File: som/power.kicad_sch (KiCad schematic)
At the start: 1 part, among them U1 XC7A200T-3FBG484E

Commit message: Mezz Power Tweak Ok
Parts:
- added C10, C11, C12, C13, C14, C15, C16, C17, C18, C19, C20, C21, C22, C23, C24, C25, C26, C27, C28, C29, C3, C30, C31, C4, C5, C6, C7, C8, C9: 100nF, Capacitor_SMD:C_0402_1005Metric_Pad0.74x0.62mm_HandSolder, symbol Device:C_Small
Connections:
- net +1V0: now also C3.1, C30.1, C31.1, C4.1, C5.1, C6.1, C7.1, C8.1, C9.1
- net +1V35: now also C12.1, C13.1, C14.1, C15.1, C16.1, C17.1
- net +1V8: now also C10.1, C11.1
- net +3V3: now also C27.1
- net GND: now also C10.2, C11.2, C12.2, C13.2, C14.2, C15.2, C16.2, C17.2, C18.2, C19.2, C20.2, C21.2, C22.2, C23.2, C24.2, C25.2, C26.2, C27.2, C28.2, C29.2, C3.2, C30.2, C31.2, C4.2, C5.2, C6.2, C7.2, C8.2, C9.2
- net VBANK13: now also C28.1, C29.1
- net VBANK14: now also C24.1, C25.1, C26.1
- net VBANK15: now also C21.1, C22.1, C23.1
- net VBANK16: now also C18.1, C19.1, C20.1
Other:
- moved on the sheet: U1J

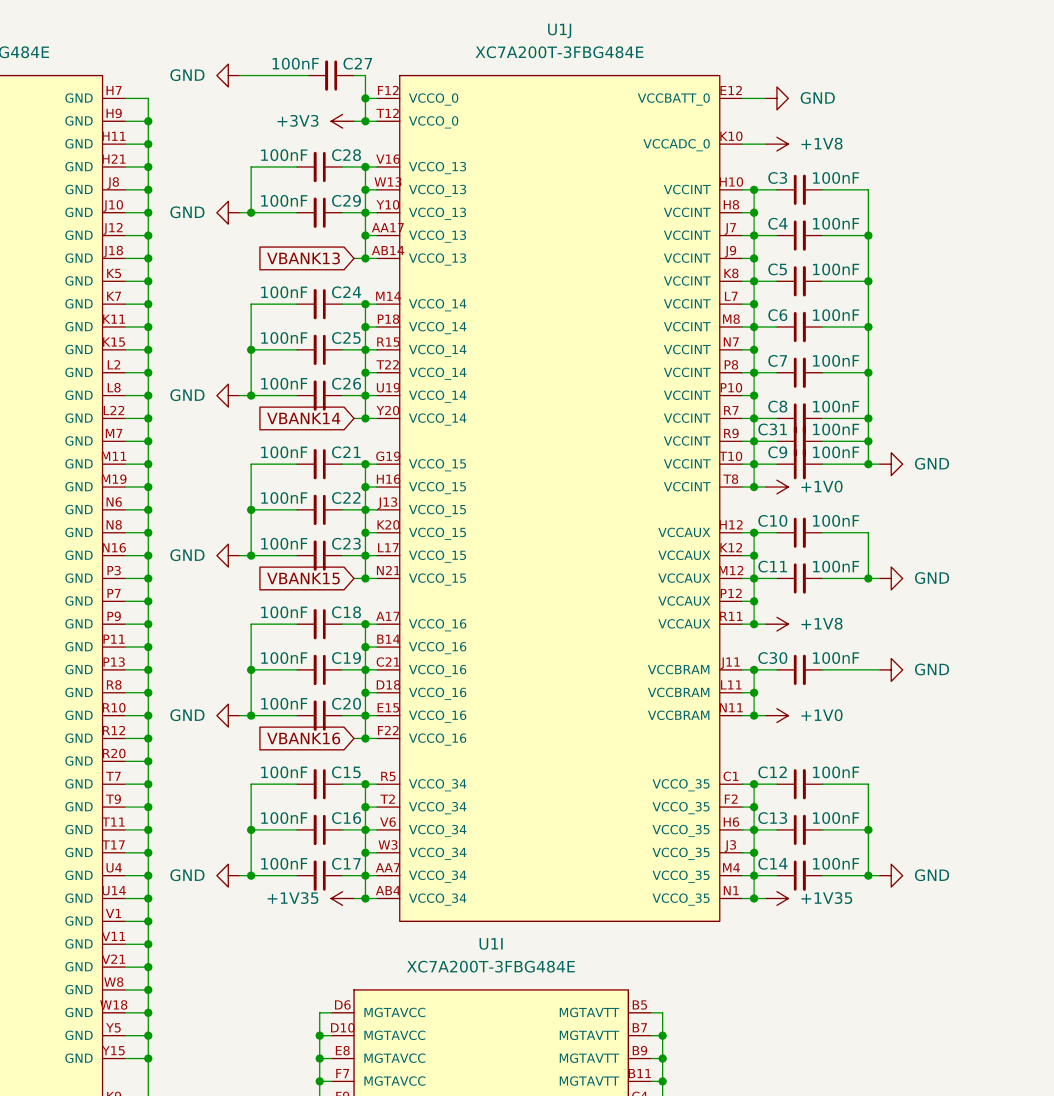
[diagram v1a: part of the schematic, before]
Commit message: Le DDR3 control traces
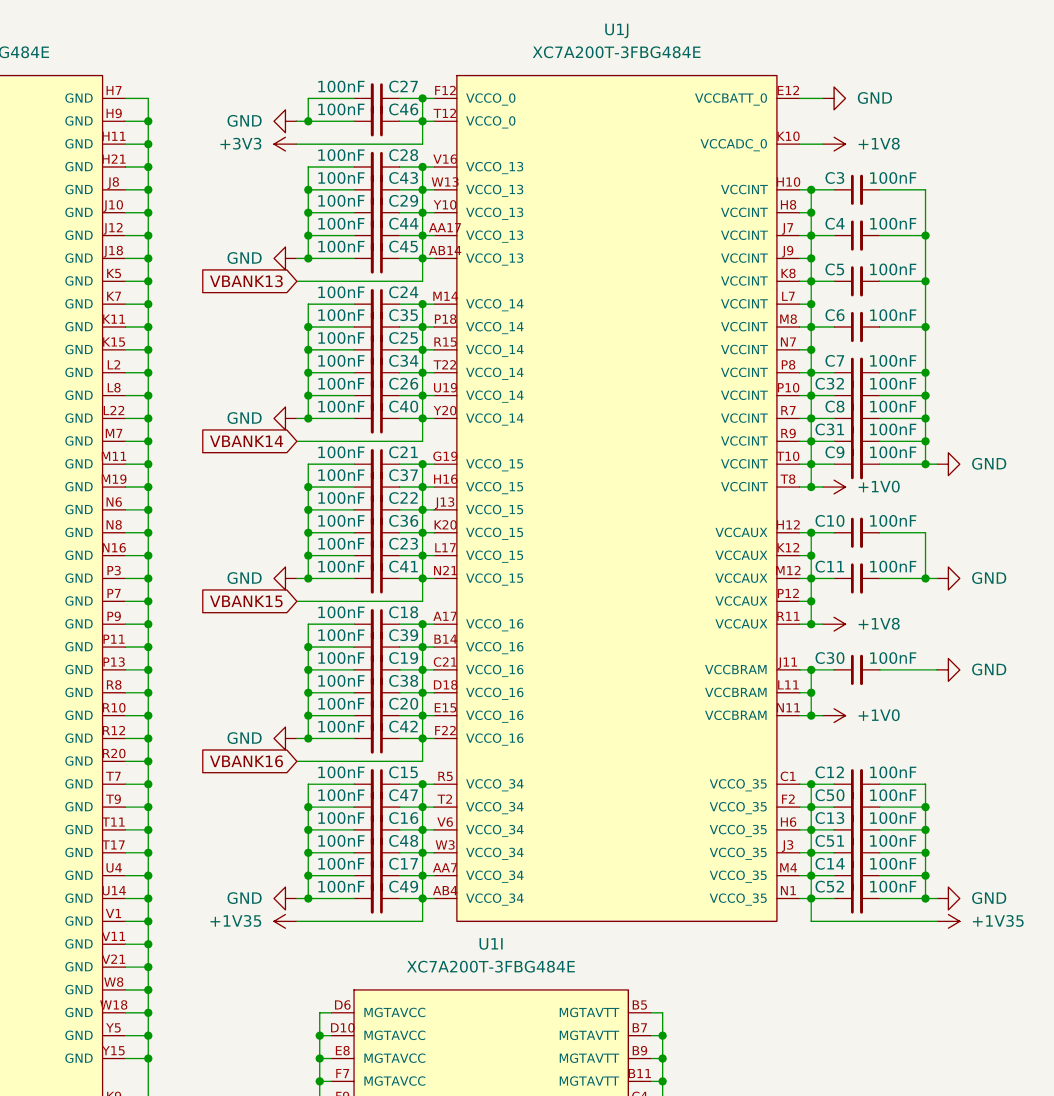
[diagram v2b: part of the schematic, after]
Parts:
- added C32, C34, C35, C36, C37, C38, C39, C40, C41, C42, C43, C44, C45, C46, C47, C48, C49, C50, C51, C52: 100nF, Capacitor_SMD:C_0402_1005Metric, symbol Device:C_Small
- C10, C11, C12, C13, C14, C15, C16, C17, C18, C19, C20, C21, C22, C23, C24, C25, C26, C27, C28, C29, C3, C30, C31, C4, C5, C6, C7, C8, C9: footprint Capacitor_SMD:C_0402_1005Metric_Pad0.74x0.62mm_HandSolder -> Capacitor_SMD:C_0402_1005Metric
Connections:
- net +1V0: now also C32.1
- net +1V35: now also C47.1, C48.1, C49.1, C50.1, C51.1, C52.1
- net +3V3: now also C46.1
- net GND: now also C32.2, C34.2, C35.2, C36.2, C37.2, C38.2, C39.2, C40.2, C41.2, C42.2, C43.2, C44.2, C45.2, C46.2, C47.2, C48.2, C49.2, C50.2, C51.2, C52.2
- net VBANK13: now also C43.1, C44.1, C45.1
- net VBANK14: now also C34.1, C35.1, C40.1
- net VBANK15: now also C36.1, C37.1, C41.1
- net VBANK16: now also C38.1, C39.1, C42.1
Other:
- moved on the sheet: C10, C11, C12, C13, C14, C15, C16, C17, C18, C19, C20, C21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

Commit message: I really should commit when I make it and not a month later
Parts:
- added C58, C59, C60, C61, C62: 100nF, Capacitor_SMD:C_0402_1005Metric, symbol Device:C_Small
- added C63: 1500uF, Capacitor_SMD:CP_Elec_10x10.5, symbol Device:C_Polarized_Small
- added C64, C65, C66, C67, C68, C69, C70, C71, C72, C73, C74, C75, C76, C77, C78, C79, C80, C81, C82, C83, C84, C85: 10uF, Capacitor_SMD:C_0402_1005Metric, symbol Device:C_Small
- added L1, L2: 2uH, Inductor_SMD:L_7.3x7.3_H3.5, symbol Device:L_Small
- added R10, R6: 75K, Resistor_SMD:R_0402_1005Metric_Pad0.72x0.64mm_HandSolder, symbol Device:R_Small
- added R11, R12, R13, R14, R9: 20K, Resistor_SMD:R_0402_1005Metric_Pad0.72x0.64mm_HandSolder, symbol Device:R_Small
- added R7: 300K, Resistor_SMD:R_0402_1005Metric_Pad0.72x0.64mm_HandSolder, symbol Device:R_Small
- added R8: 30K, Resistor_SMD:R_0402_1005Metric_Pad0.72x0.64mm_HandSolder, symbol Device:R_Small
- added U5: SIC402, SIC402:SIC402, symbol SIC402:SIC402
- added U6: TLV62569PDRLR, Package_SON:WSON-6_1.5x1.5mm_P0.5mm, symbol Regulator_Switching:TLV62569DDC
- C10, C11, C12, C13, C14, C15, C16, C17, C18, C19, C20, C21, C22, C23, C24, C25, C26, C27, C28, C29, C3, C30, C31, C32, C34, C35, C36, C37, C38, C39, C4, C40, C41, C42, C43, C44, C45, C46, C47, C48, C49, C5, C50, C51, C52, C6, C7, C8, C9: value 100nF -> 10uF
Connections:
- net +1V0: now also C63.1, C64.1, C65.1, C66.1, C67.1, C68.1, C69.1, C70.1, C75.1, C76.1, C77.1, C78.1, C79.1, L1.2, R9.2, U5.2 (VOUT)
- net +1V2: now also C80.1, C81.1, C82.1, C83.1, C84.1, C85.1
- net +1V8: now also C71.1, C72.1, C73.1, C74.1
- net +3V3: now also C61.1, C62.1, L2.2, R13.2
- net GND renamed AGND
- net AGND: now also C59.2, C60.2, C62.2, C63.2, C64.2, C65.2, C66.2, C67.2, C68.2, C69.2, C70.2, C71.2, C72.2, C73.2, C74.2, C75.2, C76.2, C77.2, C78.2, C79.2, C80.2, C81.2, C82.2, C83.2, C84.2, C85.2, R14.1, R7.1, R8.1, U5.15 (PNGD), U5.16 (PNGD), U5.17 (PNGD), U5.18 (PNGD), U5.19 (PNGD), U5.20 (PNGD), U5.21 (PNGD), U5.22 (PNGD), U5.30 (AGND), U5.32 (ENL), U5.33 (AGND), U5.4 (AGND), U6.2 (GND)
- new net: R10.1, U5.8 (BST)
- new net: R10.2, U5.13 (LXBST)
- new net: R6.1, R7.2
- new net: R6.2, U5.31 (TON)
- new net: C61.2, R13.1, R14.2, U6.6 (FB)
- new net: L2.1, U6.3 (SW)
- new net: R8.2, R9.1, U5.1 (FB)
- new net: C59.1, U5.7 (SS)
- new net: C58.1, U5.28 (LXS)
- new net: C58.2, U5.27 (ILIM)
- new net: L1.1, U5.23 (LX), U5.24 (LX), U5.25 (LX), U5.35 (LX)
- new net P_{good,1v0}: R11.2, U5.26 (PGOOD)
- new net P_{good,1v8}: R12.2, U6.1 (EN)
- new net P_{good,3v3}: U6.5 (PG)
- new net VIN: C60.1, R11.1, R12.1, U5.10 (VIN), U5.11 (VIN), U5.3 (VDD), U5.34 (VIN), U5.6 (VIN), U5.9 (VIN), U6.4 (VIN)
- no-connect marks 0 -> 2
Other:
- note added: "Main SMP targets: V_{out} = 1.0V I_{ripple} = 1.0A f_{sw} = 500kHz SIC402 formulas: V_{out} = 0.6 * (1 + R_{1}/R_{2}) k = (V_{DD} - 1.75) * 10 / V_{in} R_{ton} = k / 25 pF / f_{sw} t_{on} = V_{out} / V_{in,max} / f_{SW} L = (V_{in} - V_{out}) * t_{on} / I_{ripple} Evaluated: R_{1}/R_{2} = 0.666666667 ~= 20k/30k k = 4.696969697 ~= 4.7 R_{ton} = 375757.575757576 ~= 375k t_{on} = 0.000000606 ~= 60.6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"
- note added: "Power rail summary: - 5.0 v 3.0 A input - 3.3 v 0.5 A output - 1.8 v 0.5 A output - 1.35 v 0.5 A output - 1.2 v 0.5 A output - 1.0 v 10.0 A local"
- note added: "Power sequencing: - 1v0 - 1v8 - 1v35, 1v2, 3v3"
- moved on the sheet: C10, C11, C12, C13, C14, C15, C16, C17, C18, C19, C20, C21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

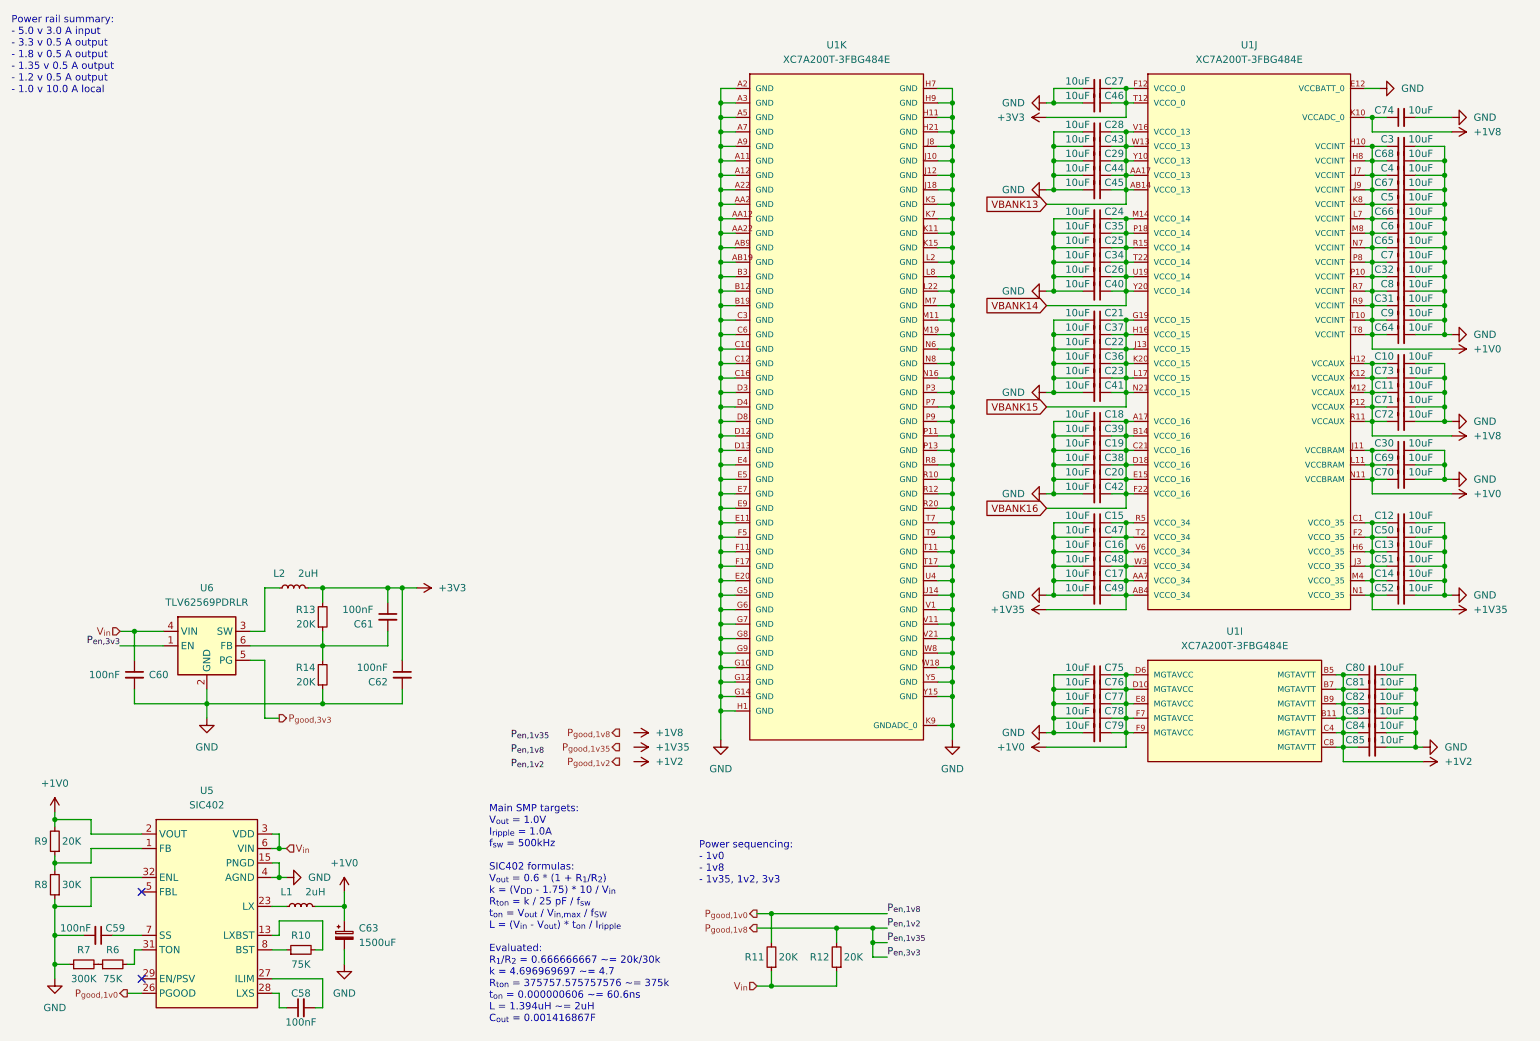
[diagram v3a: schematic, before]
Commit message: Fix the capacitor problem
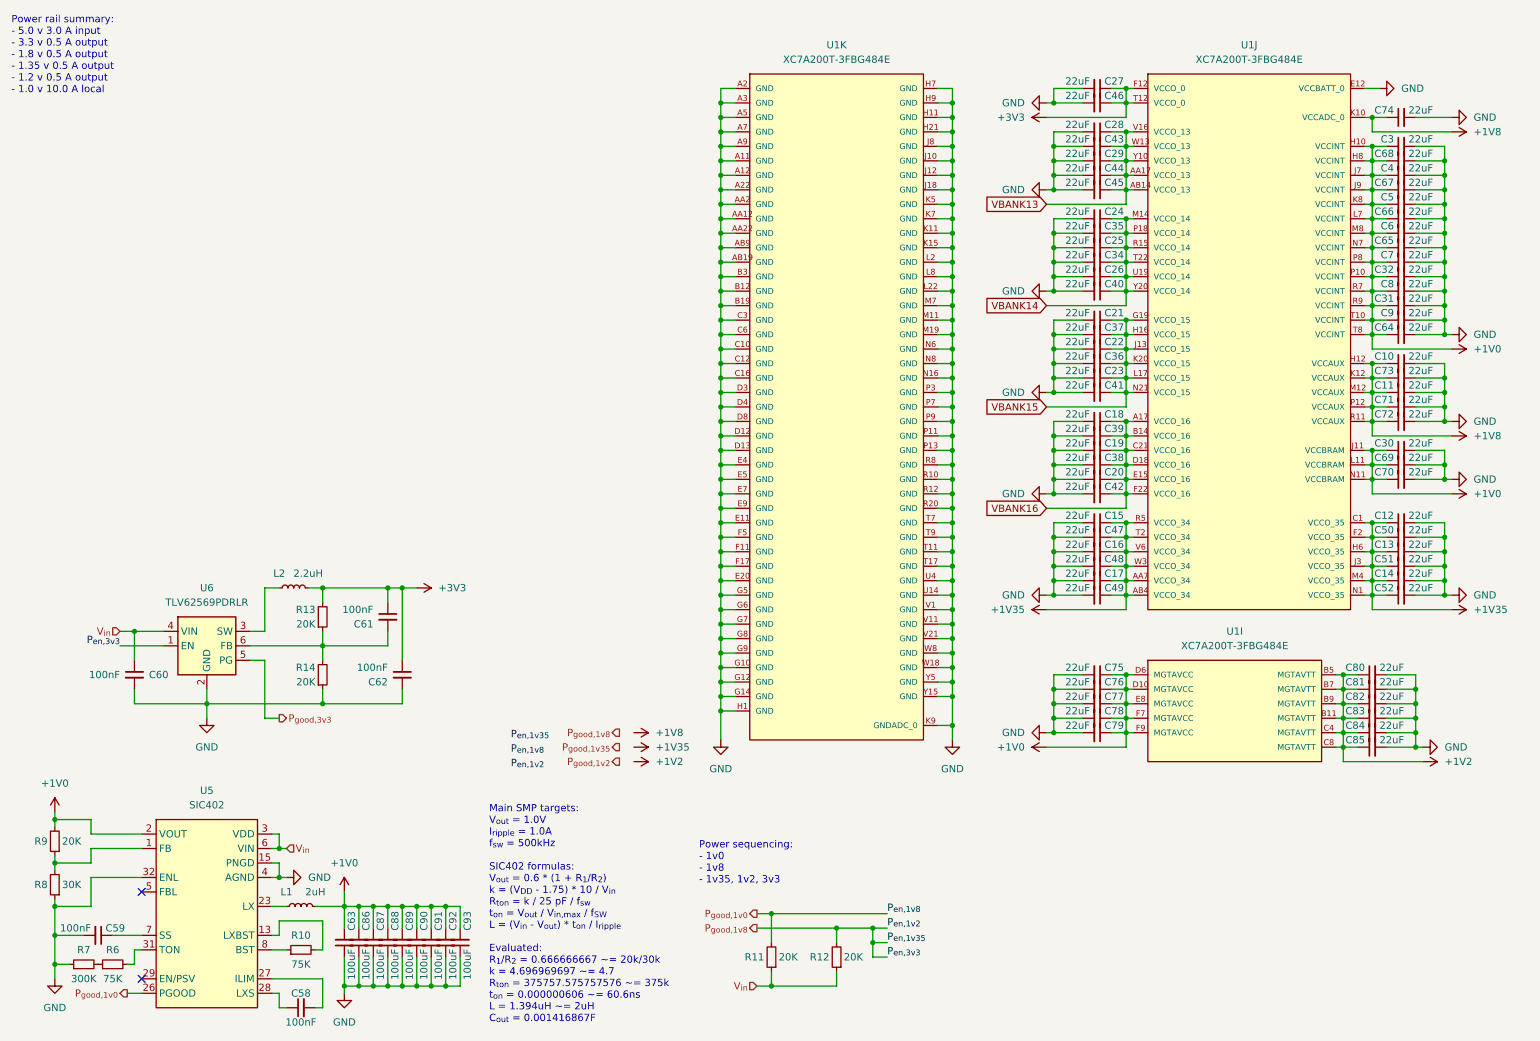
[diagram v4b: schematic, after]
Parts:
- removed C63: 1500uF, Capacitor_SMD:CP_Elec_10x10.5, symbol Device:C_Polarized_Small
- added C63, C86, C87, C88, C89, C90, C91, C92, C93: 100uF, Capacitor_SMD:C_1206_3216Metric, symbol Device:C_Small
- C10, C11, C12, C13, C14, C15, C16, C17, C18, C19, C20, C21, C22, C23, C24, C25, C26, C27, C28, C29, C3, C30, C31, C32, C34, C35, C36, C37, C38, C39, C4, C40, C41, C42, C43, C44, C45, C46, C47, C48, C49, C5, C50, C51, C52, C6, C64, C65, C66, C67, C68, C69, C7, C70, C71, C72, C73, C74, C75, C76, C77, C78, C79, C8, C80, C81, C82, C83, C84, C85, C9: value 10uF -> 22uF
- L2: value 2uH -> 2.2uH; footprint Inductor_SMD:L_7.3x7.3_H3.5 -> Inductor_SMD:L_0603_1608Metric
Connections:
- net +1V0: now also C63.2, C86.2, C87.2, C88.2, C89.2, C90.2, C91.2, C92.2, C93.2
- net AGND: now also C63.1, C86.1, C87.1, C88.1, C89.1, C90.1, C91.1, C92.1, C93.1

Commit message: ok
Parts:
- added C94, C95, C96: 100nF, Capacitor_SMD:C_0402_1005Metric, symbol Device:C_Small
- added L3, L4: 2.2uH, Inductor_SMD:L_0603_1608Metric, symbol Device:L_Small
- added R15: 20K, Resistor_SMD:R_0402_1005Metric_Pad0.72x0.64mm_HandSolder, symbol Device:R_Small
- added R16: 10K, Resistor_SMD:R_0402_1005Metric_Pad0.72x0.64mm_HandSolder, symbol Device:R_Small
- added U7, U8: TLV62569PDRLR, Package_TO_SOT_SMD:SOT-563, symbol Regulator_Switching:TLV62569DRL
- R12: value 20K -> 16K
- U6: footprint Package_SON:WSON-6_1.5x1.5mm_P0.5mm -> Package_TO_SOT_SMD:SOT-563; symbol Regulator_Switching:TLV62569DDC -> Regulator_Switching:TLV62569DRL
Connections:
- net P_{good,3v3} is gone; now on net VIN: U6.5 (EN)
- net +1V2: now also C62.1, L2.2, R13.2
- net +1V35: now also R11.2, C94.1, L3.2
- net +1V8: now also C96.1, L4.2, R15.2
- net +3V3: no longer C61.1, C62.1, L2.2, R13.2
- net AGND: now also C61.2, R12.1, C94.2, C95.2, C96.2, R16.1, U7.2 (GND), U8.2 (GND)
- net P_{good,1v0}: no longer R11.2
- net VIN: now also C61.1, U6.3 (VIN), C95.1, U7.3 (VIN), U7.5 (EN), U8.3 (VIN), U8.5 (EN); no longer R11.1, R12.1, U6.4 (VIN)
- net at R13.1, R14.2: now also U6.1 (FB); no longer C61.2, U6.6 (FB)
- net at L2.1: now also U6.4 (SW); no longer U6.3 (SW)
- net P_{good,1v8}: no longer names the net of R12.2
- net P_{good,1v8}: now also R11.1, U7.1 (FB); no longer U6.1 (EN)
- new net: L4.1, U8.4 (SW)
- new net: R15.1, R16.2, U8.1 (FB)
- new net: L3.1, U7.4 (SW)
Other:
- note added: "Power rail summary: - 5.0 v 3.0 A input - 3.3 v 0.5 A input - 1.8 v 0.5 A local - 1.35 v 0.5 A local - 1.2 v 0.5 A output - 1.0 v 10.0 A local / 0.5 A output"
- note removed: "Power rail summary: - 5.0 v 3.0 A input - 3.3 v 0.5 A output - 1.8 v 0.5 A output - 1.35 v 0.5 A output - 1.2 v 0.5 A output - 1.0 v 10.0 A local"
- note removed: "Power sequencing: - 1v0 - 1v8 - 1v35, 1v2, 3v3"
- moved on the sheet: C62

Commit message: Work on GTP and power supplies for it
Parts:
- removed C60, C62: 100nF, Capacitor_SMD:C_0402_1005Metric, symbol Device:C_Small
- removed L2: 2.2uH, Inductor_SMD:L_0603_1608Metric, symbol Device:L_Small
- removed U6: TLV62569PDRLR, Package_TO_SOT_SMD:SOT-563, symbol Regulator_Switching:TLV62569DRL
- added R20: 160K, Resistor_SMD:R_0402_1005Metric_Pad0.72x0.64mm_HandSolder, symbol Device:R_Small
- added R21: 77K, Resistor_SMD:R_0402_1005Metric_Pad0.72x0.64mm_HandSolder, symbol Device:R_Small
- added U10, U6: RS3236-ADJ8YF5, Package_TO_SOT_SMD:TSOT-23-5, symbol Regulator_Linear:ADP7142AUJZ
- R13: value 20K -> 37K5
- R14: value 20K -> 160K
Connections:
- net +1V0: no longer C75.1, C76.1, C77.1, C78.1, C79.1, U1.D10 (MGTAVCC), U1.D6 (MGTAVCC), U1.E8 (MGTAVCC), U1.F7 (MGTAVCC), U1.F9 (MGTAVCC)
- net +3V3: now also U10.1 (VIN), U10.3 (EN), U6.1 (VIN), U6.3 (EN)
- net AGND: now also R13.1, R21.1, U10.2 (GND), U6.2 (GND); no longer R14.1
- net MTGAVCC: now reaches R14.2
- net MTGAVCC: now also C75.1, C76.1, C77.1, C78.1, C79.1, U1.D10 (MGTAVCC), U1.D6 (MGTAVCC), U1.E8 (MGTAVCC), U1.F7 (MGTAVCC), U1.F9 (MGTAVCC), U6.5 (VOUT); no longer R13.1
- net +1V2 renamed MTGAVTT
- net MTGAVTT: now also R20.2, U10.5 (VOUT); no longer R13.2
- new net: R13.2, R14.1, U6.4 (SENSE/ADJ)
- new net: R20.1, R21.2, U10.4 (SENSE/ADJ)
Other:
- note added: "Power rail summary: - 5.0 v 3.0 A input - 3.3 v 0.5 A input - 1.8 v 0.5 A local - 1.35 v 0.5 A local - 1.2 v 0.5 A output (for MTGAVTT) - 1.0 v 0.5 A output (for MTGAVCC) - 1.0 v 10.0 A local / 0.5 A output"
- note removed: "Power rail summary: - 5.0 v 3.0 A input - 3.3 v 0.5 A input - 1.8 v 0.5 A local - 1.35 v 0.5 A local - 1.2 v 0.5 A output - 1.0 v 10.0 A local / 0.5 A output"
- moved on the sheet: C75, C76, C77, C78, C79, C80, C81, C82, C83, C84, C85, U1I

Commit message: idk
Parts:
- U1: LCSC part number (none) -> C1521841; automotive No -> (none); category IC -> (none); device class L1 Integrated Circuits (ICs) -> (none); device class L2 Embedded Processors and Controllers -> (none); device class L3 FPGAs - Field Programmable Gate Arrays -> (none); digikey description IC FPGA ARTIX7 285 I/O 484FCBGA -> (none); lead free Yes -> (none); max supply voltage 3.465V -> (none); min supply voltage 0.95V -> (none); number of I/Os 285 -> (none); number of logic blocks 33650 -> (none); number of logic elements cells 215360 -> (none); package FBG484 -> (none); release date 1402480027 -> (none); rohs Yes -> (none); speed grade 3 -> (none); standoff height 0.4mm -> (none); temperature range high +100°C -> (none); temperature range low 0°C -> (none); vault revision 8A58598F-56A5-4DEC-BA3F-FDB4B6026E25 -> (none)
- U10, U6: LCSC part number (none) -> C379351
- U5: LCSC part number (none) -> C511100
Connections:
- net P_{good,1v0}: no longer names the net of U5.26 (PGOOD)
- no-connect marks 2 -> 3
